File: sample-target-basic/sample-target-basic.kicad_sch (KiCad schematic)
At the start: 35 parts, among them J1 USB_C_Receptacle, J2 Conn_01x03, SW1 SW_Push, SW2 SW_Push, U1 MIC5504-3.3YM5, U2 W25Q128JVS, U3 RP2040, Y1 ABM8-272-T3

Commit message: Various fixes while ordering from JLCPCB
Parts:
- J1: LCSC C134092 -> C2761408
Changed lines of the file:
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@@
 			)
 		)
-		(property "LCSC" "C134092"
+		(property "LCSC" "C2761408"
 			(at 45.72 71.12 0)
 			(effects

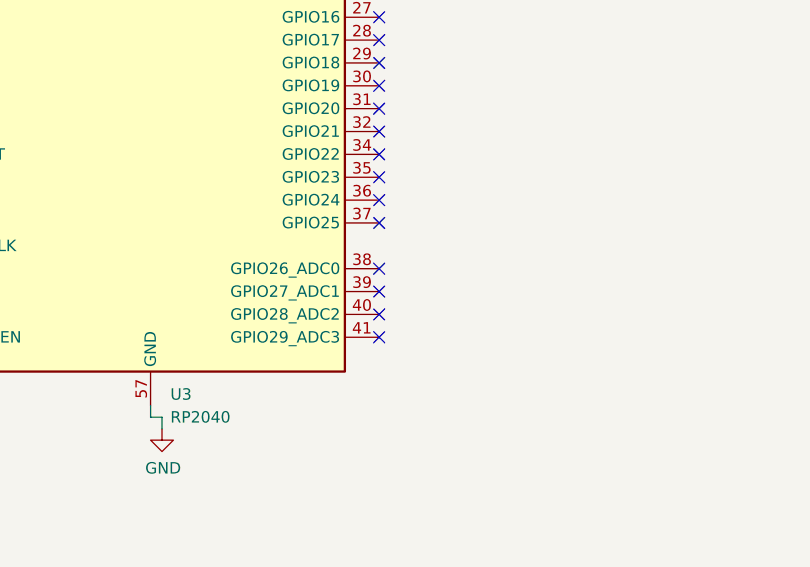
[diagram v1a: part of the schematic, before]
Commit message: Add CC lines to sample targets
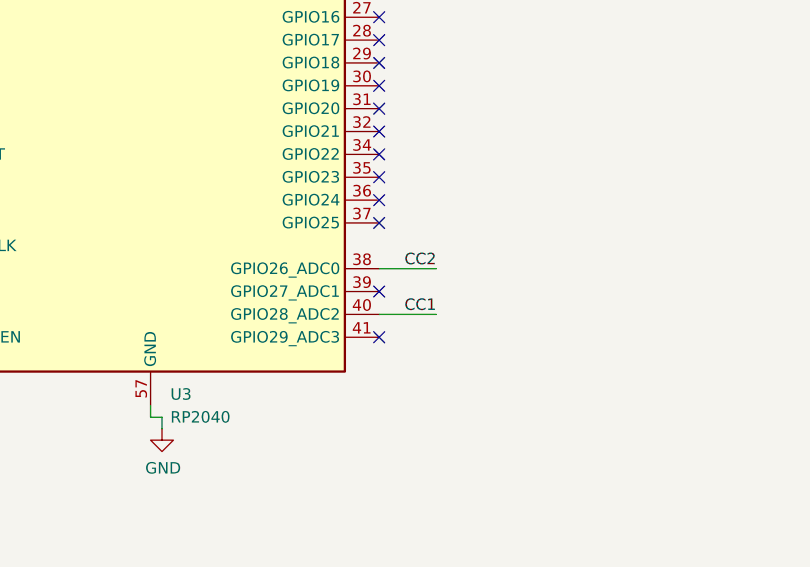
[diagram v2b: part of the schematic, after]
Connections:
- net CC1: now also U3.40 (GPIO28_ADC2)
- net CC2: now also U3.38 (GPIO26_ADC0)
- no-connect marks 32 -> 30
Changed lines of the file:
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@@
 	(title_block
 		(title "SWD2USBC Sample Target (Basic)")
-		(date "2025-01-05")
-		(rev "v1.0")
+		(date "2025-02-16")
+		(rev "v1.1")
 		(company "alvarop.com")
 	)
@@
 	)
 	(no_connect
-		(at 325.12 144.78)
-	)
-	(no_connect
 		(at 60.96 71.12)
 	)
@@
 	)
 	(no_connect
-		(at 325.12 139.7)
-	)
-	(no_connect
 		(at 60.96 88.9)
 	)
@@
 	(wire
 		(pts
+			(xy 325.12 139.7) (xy 331.47 139.7)
+		)
+		(stroke
+			(width 0)
+			(type default)
+		)
+	)
+	(wire
+		(pts
 			(xy 259.08 116.84) (xy 274.32 116.84)
 		)
@@
 		(pts
 			(xy 259.08 137.16) (xy 274.32 137.16)
+		)
+		(stroke
+			(width 0)
+			(type default)
+		)
+	)
+	(wire
+		(pts
+			(xy 325.12 144.78) (xy 331.47 144.78)
 		)
 		(stroke
@@
 	(label "QSPI_SD3"
 		(at 259.08 101.6 0)
-		(fields_autoplaced yes)
 		(effects
 			(font
@@
 	(label "CC2"
 		(at 99.06 53.34 180)
-		(fields_autoplaced yes)
 		(effects
 			(font
@@
 	(label "SWD"
 		(at 259.08 139.7 0)
-		(fields_autoplaced yes)
 		(effects
 			(font
@@
 	(label "USB_D+"
 		(at 236.22 73.66 0)
-		(fields_autoplaced yes)
 		(effects
 			(font
@@
 	(label "QSPI_SS"
 		(at 259.08 88.9 0)
-		(fields_autoplaced yes)
 		(effects
 			(font
@@
 	(label "CC1"
 		(at 99.06 50.8 180)
-		(fields_autoplaced yes)
 		(effects
 			(font
@@
 	(label "QSPI_SD0"
 		(at 259.08 93.98 0)
-		(fields_autoplaced yes)
 		(effects
 			(font
@@
 	(label "USB_D+"
 		(at 73.66 66.04 180)
-		(fields_autoplaced yes)
 		(effects
 			(font
@@
 	(label "USB_D-"
 		(at 73.66 60.96 180)
-		(fields_autoplaced yes)
 		(effects
 			(font
@@
 	(label "RUN"
 		(at 259.08 71.12 0)
-		(fields_autoplaced yes)
 		(effects
 			(font
@@
 	(label "XIN"
 		(at 259.08 116.84 0)
-		(fields_autoplaced yes)
 		(effects
 			(font
@@
 	(label "~{USB_BOOT}"
 		(at 173.99 142.24 0)
-		(fields_autoplaced yes)
 		(effects
 			(font
@@
 	(label "QSPI_SD3"
 		(at 200.66 154.94 0)
-		(fields_autoplaced yes)
 		(effects
 			(font
@@
 	(label "QSPI_SCLK"
 		(at 200.66 144.78 0)
-		(fields_autoplaced yes)
 		(effects
 			(font
@@
 	(label "LED2"
 		(at 349.25 92.71 0)
-		(fields_autoplaced yes)
 		(effects
 			(font
@@
 	(label "XOUT"
 		(at 259.08 127 0)
-		(fields_autoplaced yes)
 		(effects
 			(font
@@
 	(label "UART0_TX"
 		(at 344.17 71.12 180)
-		(fields_autoplaced yes)
 		(effects
 			(font
@@
 	(label "SWD"
 		(at 73.66 81.28 180)
-		(fields_autoplaced yes)
+		(effects
+			(font
+				(size 1.27 1.27)
+			)
+			(justify right bottom)
+		)
+	)
+	(label "CC2"
+		(at 331.47 139.7 180)
 		(effects
 			(font
@@
 	(label "QSPI_SD2"
 		(at 259.08 99.06 0)
-		(fields_autoplaced yes)
 		(effects
 			(font
@@
 	(label "UART0_RX"
 		(at 344.17 73.66 180)
-		(fields_autoplaced yes)
 		(effects
 			(font
@@
 	(label "RUN"
 		(at 165.1 142.24 180)
-		(fields_autoplaced yes)
 		(effects
 			(font
@@
 	(label "LED1"
 		(at 349.25 82.55 0)
-		(fields_autoplaced yes)
 		(effects
 			(font
@@
 	(label "D-"
 		(at 262.89 83.82 0)
-		(fields_autoplaced yes)
 		(effects
 			(font
@@
 	(label "SWCLK"
 		(at 73.66 78.74 180)
-		(fields_autoplaced yes)
 		(effects
 			(font
@@
 	(label "SWO"
 		(at 73.66 93.98 180)
-		(fields_autoplaced yes)
 		(effects
 			(font
@@
 	(label "XOUT"
 		(at 320.04 191.77 180)
-		(fields_autoplaced yes)
 		(effects
 			(font
@@
 	(label "D+"
 		(at 262.89 73.66 0)
-		(fields_autoplaced yes)
 		(effects
 			(font
@@
 	(label "SWCLK"
 		(at 259.08 137.16 0)
-		(fields_autoplaced yes)
 		(effects
 			(font
@@
 	(label "QSPI_SD1"
 		(at 200.66 149.86 0)
-		(fields_autoplaced yes)
-		(effects
-			(font
-				(size 1.27 1.27)
-			)
-			(justify left bottom)
+		(effects
+			(font
+				(size 1.27 1.27)
+			)
+			(justify left bottom)
+		)
+	)
+	(label "CC1"
+		(at 331.47 144.78 180)
+		(effects
+			(font
+				(size 1.27 1.27)
+			)
+			(justify right bottom)
 		)
 	)
 	(label "QSPI_SS"
 		(at 200.66 142.24 0)
-		(fields_autoplaced yes)
 		(effects
 			(font
@@
 	(label "USB_D-"
 		(at 236.22 83.82 0)
-		(fields_autoplaced yes)
 		(effects
 			(font
@@
 	(label "QSPI_SD1"
 		(at 259.08 96.52 0)
-		(fields_autoplaced yes)
 		(effects
 			(font
@@
 	(label "XIN"
 		(at 320.04 181.61 180)
-		(fields_autoplaced yes)
 		(effects
 			(font
@@
 	(label "QSPI_SD2"
 		(at 200.66 152.4 0)
-		(fields_autoplaced yes)
 		(effects
 			(font
@@
 	(label "RUN"
 		(at 73.66 96.52 180)
-		(fields_autoplaced yes)
 		(effects
 			(font
@@
 	(label "QSPI_SD0"
 		(at 200.66 147.32 0)
-		(fields_autoplaced yes)
 		(effects
 			(font
@@
 	(label "QSPI_SCLK"
 		(at 259.08 104.14 0)
-		(fields_autoplaced yes)
-		(effects
-			(font
+		(effects
+			(font

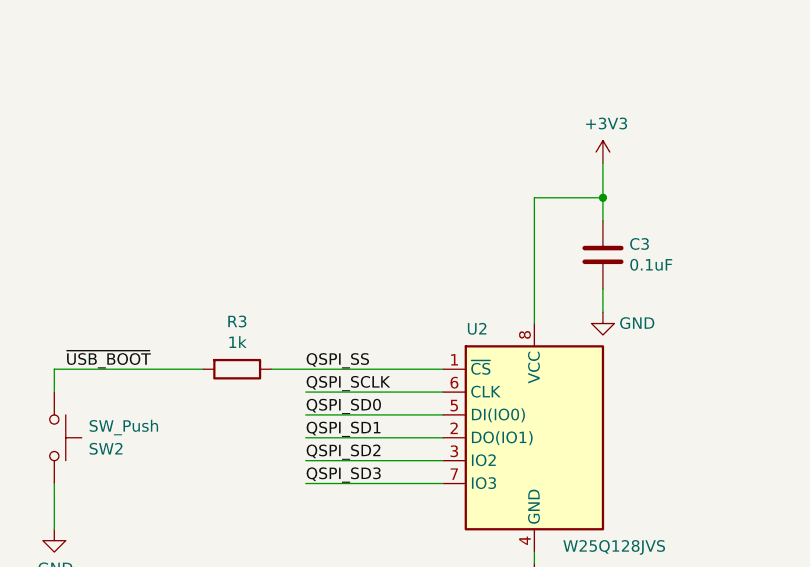
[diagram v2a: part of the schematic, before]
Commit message: Add pull up resistor to spi flash
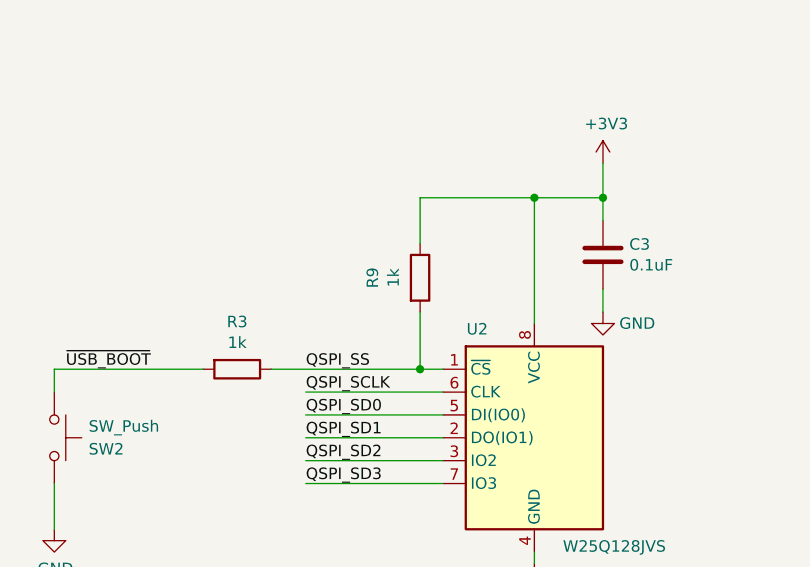
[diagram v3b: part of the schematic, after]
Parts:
- added R9: 1k, Resistor_SMD:R_0402_1005Metric, symbol Device:R
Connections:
- net +3V3: now also R9.1
- net QSPI_SS: now also R9.2
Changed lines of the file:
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@@
 	(title_block
 		(title "SWD2USBC Sample Target (Basic)")
-		(date "2025-02-16")
-		(rev "v1.1")
+		(date "2025-02-19")
+		(rev "v1.2")
 		(company "alvarop.com")
 	)
@@
 	)
 	(junction
+		(at 213.36 142.24)
+		(diameter 0)
+		(color 0 0 0 0)
+	)
+	(junction
 		(at 346.71 30.48)
 		(diameter 0)
@@
 	)
 	(junction
+		(at 226.06 123.19)
+		(diameter 0)
+		(color 0 0 0 0)
+	)
+	(junction
 		(at 233.68 123.19)
 		(diameter 0)
@@
 	(wire
 		(pts
+			(xy 213.36 135.89) (xy 213.36 142.24)
+		)
+		(stroke
+			(width 0)
+			(type default)
+		)
+	)
+	(wire
+		(pts
 			(xy 359.41 92.71) (xy 361.95 92.71)
 		)
@@
 	(wire
 		(pts
+			(xy 213.36 123.19) (xy 226.06 123.19)
+		)
+		(stroke
+			(width 0)
+			(type default)
+		)
+	)
+	(wire
+		(pts
 			(xy 259.08 127) (xy 274.32 127)
 		)
@@
 	(wire
 		(pts
+			(xy 213.36 128.27) (xy 213.36 123.19)
+		)
+		(stroke
+			(width 0)
+			(type default)
+		)
+	)
+	(wire
+		(pts
 			(xy 341.63 78.74) (xy 341.63 92.71)
 		)
@@
 	(wire
 		(pts
-			(xy 196.85 142.24) (xy 215.9 142.24)
+			(xy 196.85 142.24) (xy 213.36 142.24)
 		)
 		(stroke
@@
 	(wire
 		(pts
+			(xy 213.36 142.24) (xy 215.9 142.24)
+		)
+		(stroke
+			(width 0)
+			(type default)
+		)
+	)
+	(wire
+		(pts
 			(xy 287.02 31.75) (xy 287.02 30.48)
 		)
@@
 					(unit 1)
 				)
+			)
+		)
+	)
+	(symbol
+		(lib_id "Device:R")
+		(at 213.36 132.08 0)
+		(unit 1)
+		(exclude_from_sim no)
+		(in_bom yes)
+		(on_board yes)
+		(dnp no)
+		(property "Reference" "R9"
+			(at 208.1022 132.08 90)
+			(effects
+				(font
+					(size 1.27 1.27)
+				)
+			)
+		)
+		(property "Value" "1k"
+			(at 210.4136 132.08 90)
+			(effects
+				(font
+					(size 1.27 1.27)
+				)
+			)
+		)
+		(property "Footprint" "Resistor_SMD:R_0402_1005Metric"
+			(at 211.582 132.08 90)
+			(effects
+				(font
+					(size 1.27 1.27)
+				)
+				(hide yes)
+			)
+		)
+		(property "Datasheet" "~"
+			(at 213.36 132.08 0)
+			(effects
+				(font
+					(size 1.27 1.27)
+				)
+				(hide yes)
+			)
+		)
+		(property "Description" ""
+			(at 213.36 132.08 0)
+			(effects
+				(font
+					(size 1.27 1.27)
+				)
+				(hide yes)
+			)
+		)
+		(property "LCSC" "C4190"
+			(at 213.36 132.08 0)
+			(effects
+				(font
+					(size 1.27 1.27)
+				)
+				(hide yes)
+			)
+		)
+		(pin "1"
+		)
+		(pin "2"
+		)
+		(instances
+			(project "sample-target-basic"
+				(path "/f3846d6f-2066-409b-95b3-d044da1ab9d1"
+					(reference "R9")
+					(unit 1)
+				)
